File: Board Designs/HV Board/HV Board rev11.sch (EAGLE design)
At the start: 62 parts, among them IC1 OKI-78SR-5, IC2 NE5532SOIC

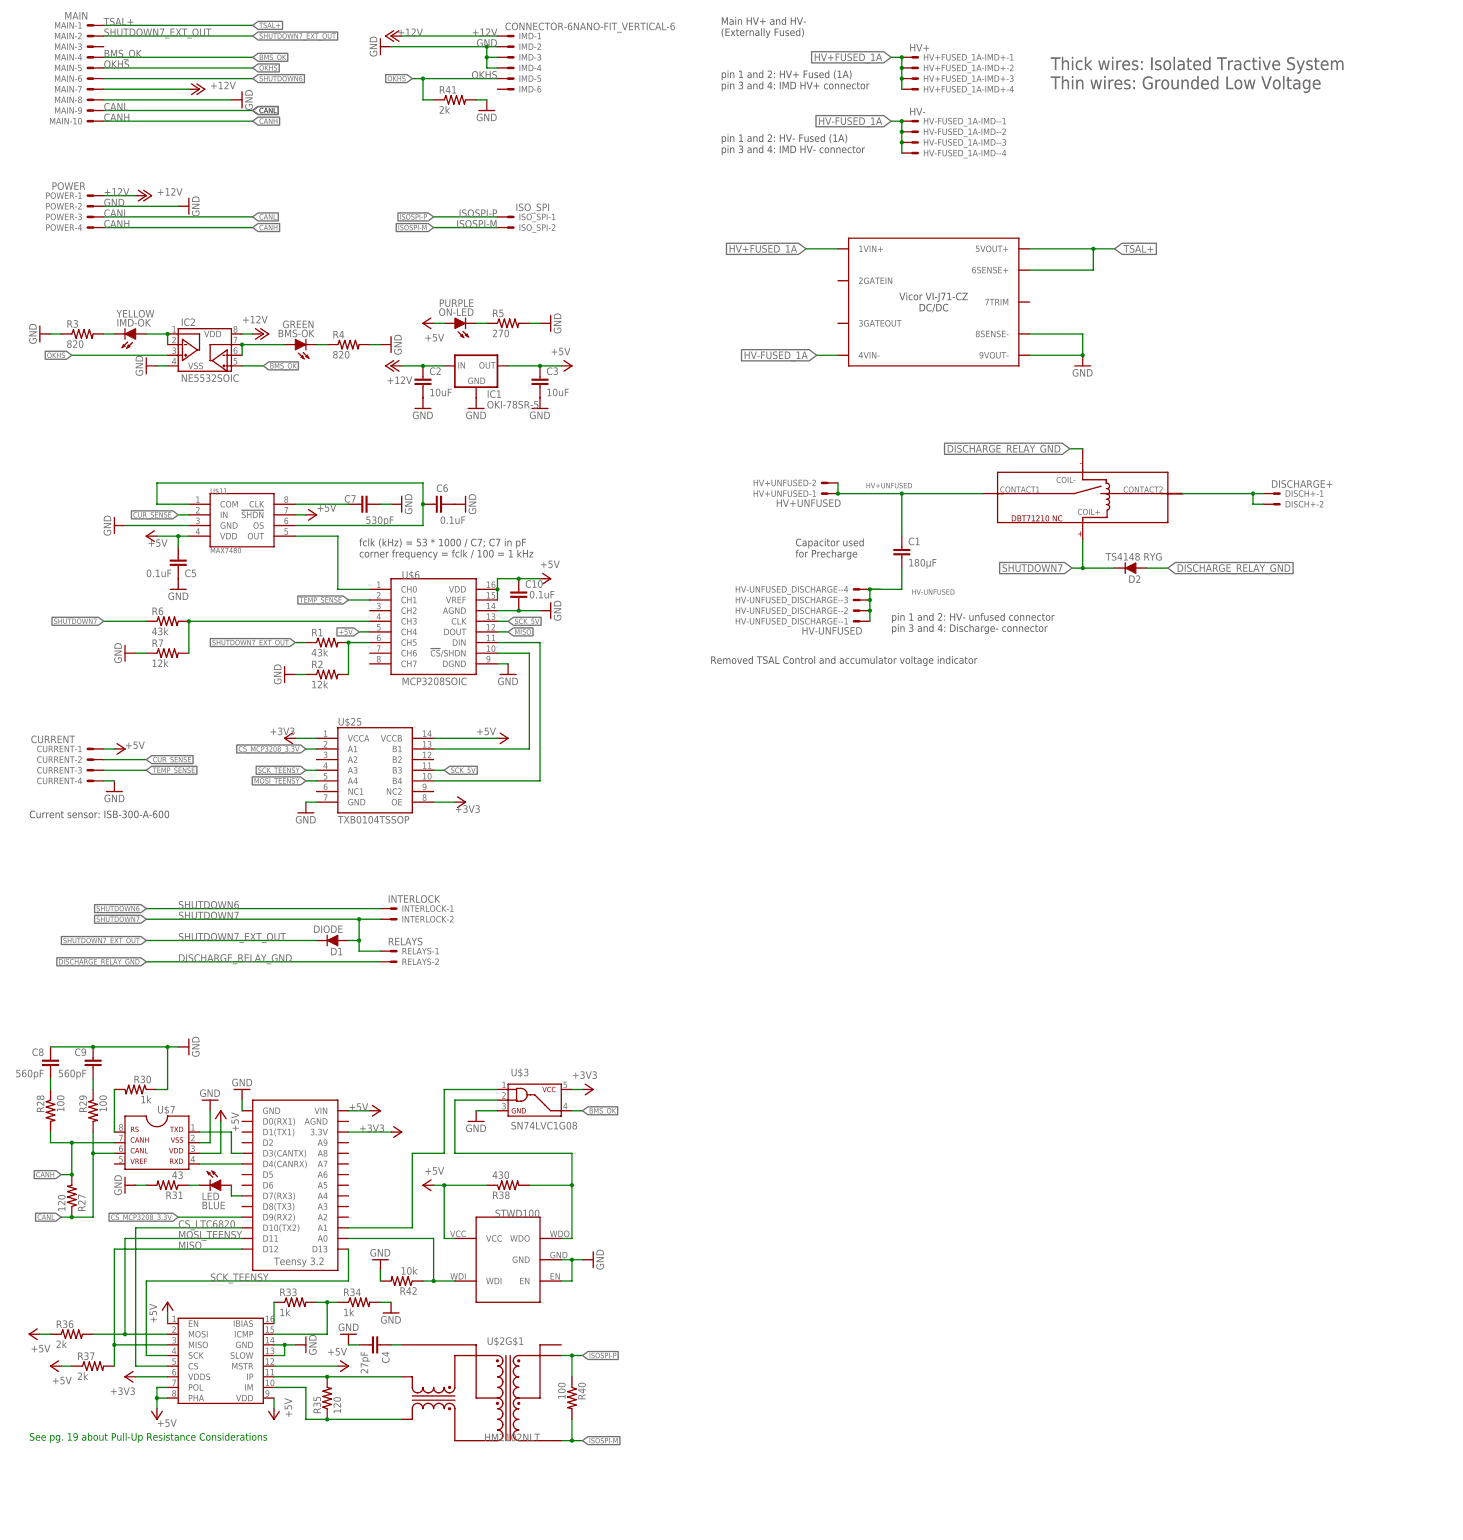
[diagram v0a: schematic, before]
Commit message: HV Board rev11: Update discharge relay holes and pads, change ADC to read shutdown_G, moved silkscreen
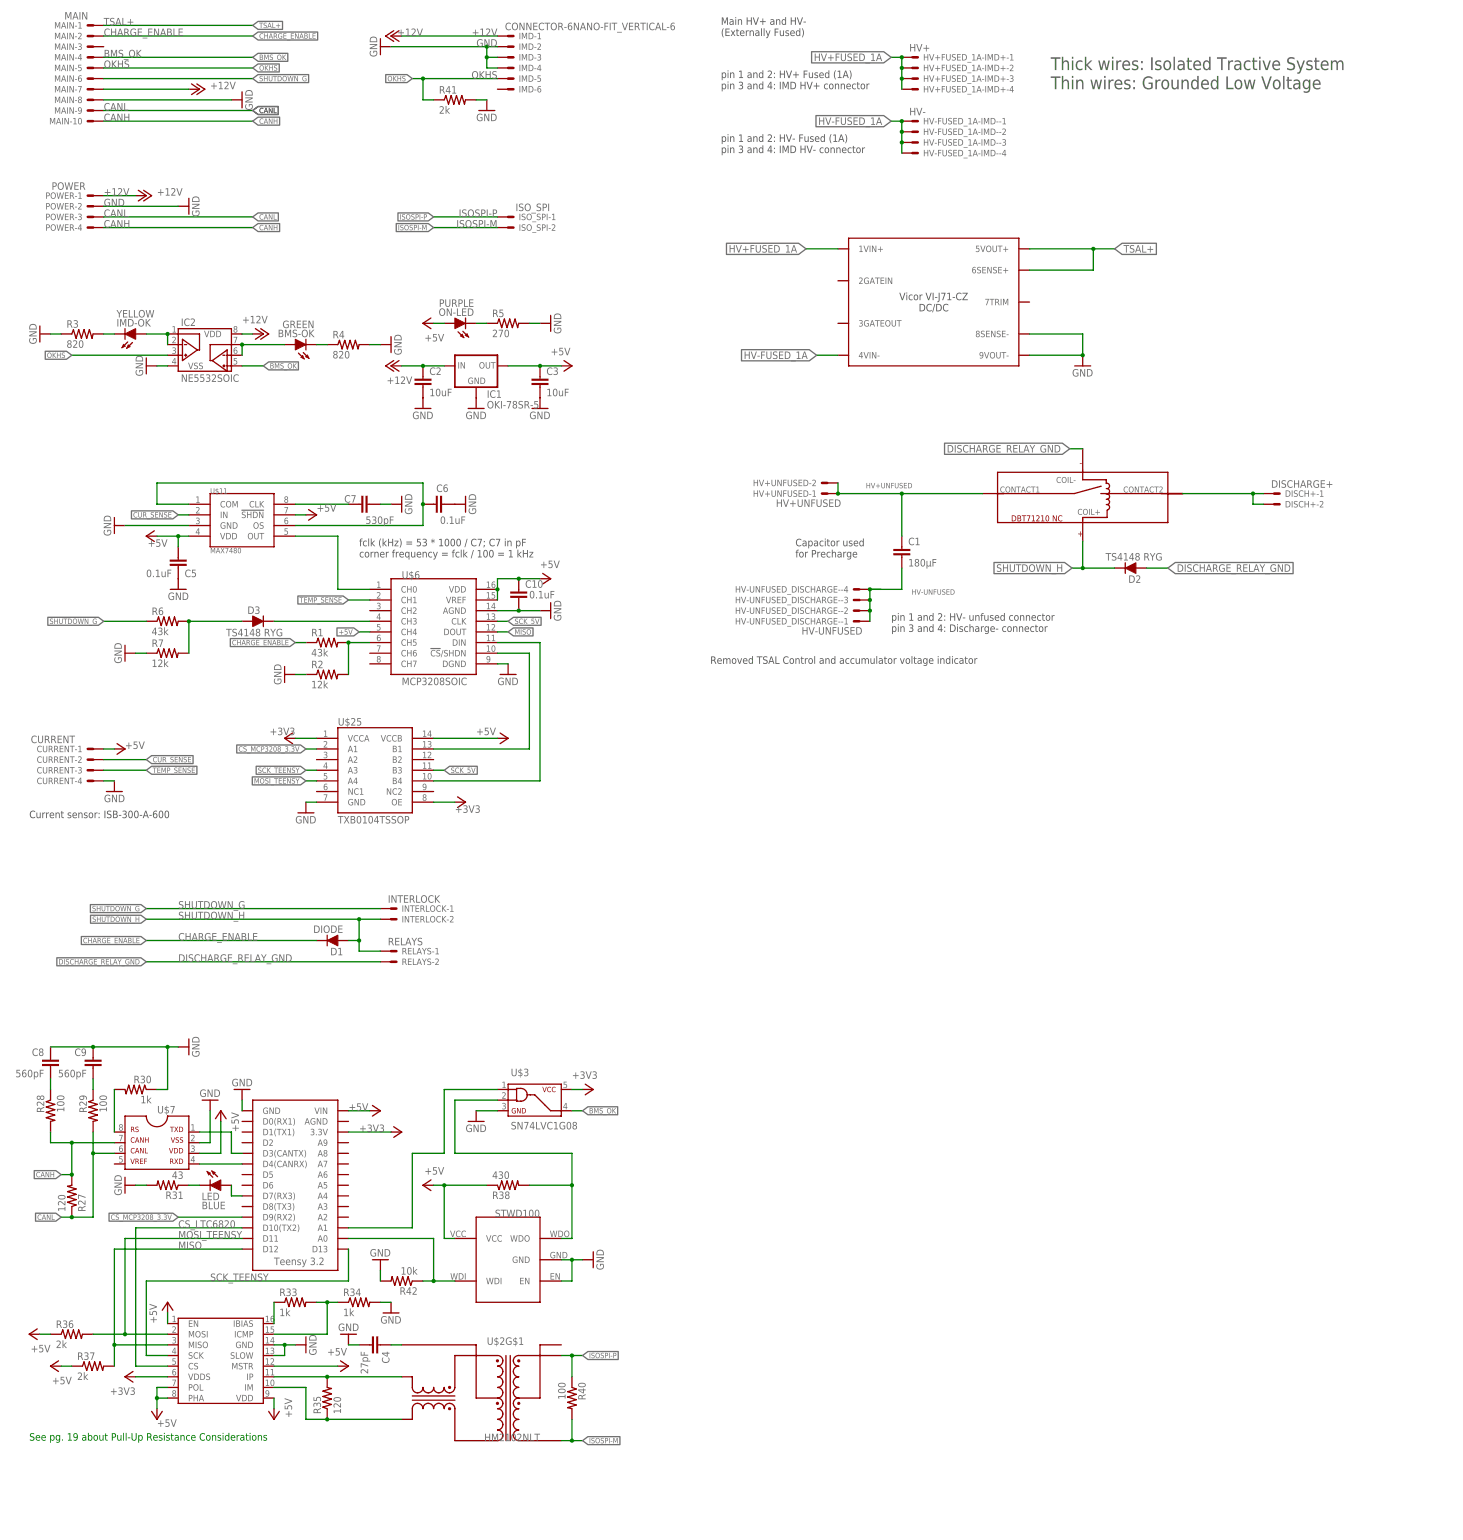
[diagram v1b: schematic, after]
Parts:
- added D3: TS4148 RYG, HyTechDevices:DIODE0805
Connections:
- net SHUTDOWN7_EXT_OUT renamed CHARGE_ENABLE
- removed net SHUTDOWN6: INTERLOCK-1.S, MAIN-6.S
- removed net SHUTDOWN7: D1.A, D2.C, INTERLOCK-2.S, R6.1, RELAYS-1.S, U$4.COIL+
- new net N$10: D3.C, U$6.CH3
- new net SHUTDOWN_G: INTERLOCK-1.S, MAIN-6.S, R6.1
- new net SHUTDOWN_H: D1.A, D2.C, INTERLOCK-2.S, RELAYS-1.S, U$4.COIL+
- net N$9: now also D3.A; no longer U$6.CH3
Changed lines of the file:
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@@
 <part name="GND20" library="supply1" deviceset="GND" device=""/>
 <part name="D2" library="HyTechDevices" deviceset="DIODE" device="0805" value="TS4148 RYG"/>
+<part name="D3" library="HyTechDevices" deviceset="DIODE" device="0805" value="TS4148 RYG"/>
 </parts>
 <sheets>
@@
 <attribute name="VALUE" x="285.75" y="-75.1586" size="1.778" layer="96" rot="R180"/>
 </instance>
+<instance part="D3" gate="1" x="71.12" y="-91.44" smashed="yes">
+<attribute name="NAME" x="67.31" y="-89.6874" size="1.778" layer="95"/>
+<attribute name="VALUE" x="62.23" y="-95.0214" size="1.778" layer="96"/>
+</instance>
 </instances>
 <busses>
@@
 </segment>
 </net>
-<net name="SHUTDOWN7" class="0">
+<net name="SHUTDOWN_H" class="0">
 <segment>
 <wire x1="266.7" y1="-78.74" x2="266.7" y2="-72.26" width="0.1524" layer="91"/>
@@
 <junction x="93.98" y="-167.64"/>
 </segment>
-<segment>
-<pinref part="R6" gate="G$1" pin="1"/>
-<wire x1="43.18" y1="-91.44" x2="33.02" y2="-91.44" width="0.1524" layer="91"/>
-<label x="33.02" y="-91.44" size="1.27" layer="95" rot="R180" xref="yes"/>
-</segment>
-</net>
-<net name="SHUTDOWN6" class="0">
+</net>
+<net name="SHUTDOWN_G" class="0">
 <segment>
 <pinref part="INTERLOCK" gate="-1" pin="S"/>
@@
 <label x="68.58" y="38.1" size="1.27" layer="95" xref="yes"/>
 </segment>
-</net>
-<net name="SHUTDOWN7_EXT_OUT" class="0">
+<segment>
+<pinref part="R6" gate="G$1" pin="1"/>
+<wire x1="43.18" y1="-91.44" x2="33.02" y2="-91.44" width="0.1524" layer="91"/>
+<label x="33.02" y="-91.44" size="1.27" layer="95" rot="R180" xref="yes"/>
+</segment>
+</net>
+<net name="CHARGE_ENABLE" class="0">
 <segment>
 <label x="33.02" y="48.26" size="1.778" layer="95"/>
@@
 <pinref part="R7" gate="G$1" pin="2"/>
 <wire x1="53.34" y1="-99.06" x2="53.34" y2="-91.44" width="0.1524" layer="91"/>
+<pinref part="D3" gate="1" pin="A"/>
+<wire x1="53.34" y1="-91.44" x2="66.04" y2="-91.44" width="0.1524" layer="91"/>
 <junction x="53.34" y="-91.44"/>
+</segment>
+</net>
+<net name="N$10" class="0">
+<segment>
+<pinref part="D3" gate="1" pin="C"/>
 <pinref part="U$6" gate="G$1" pin="CH3"/>
-<wire x1="53.34" y1="-91.44" x2="96.52" y2="-91.44" width="0.1524" layer="91"/>
-</segment>
-</net>
+<wire x1="73.66" y1="-91.44" x2="96.52" y2="-91.44" width="0.1524" layer="91"/>
+</segment>
+</net>

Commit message: HV Board rev11: Amplified BMS_OK signal, added split CAN termination and TVS diode
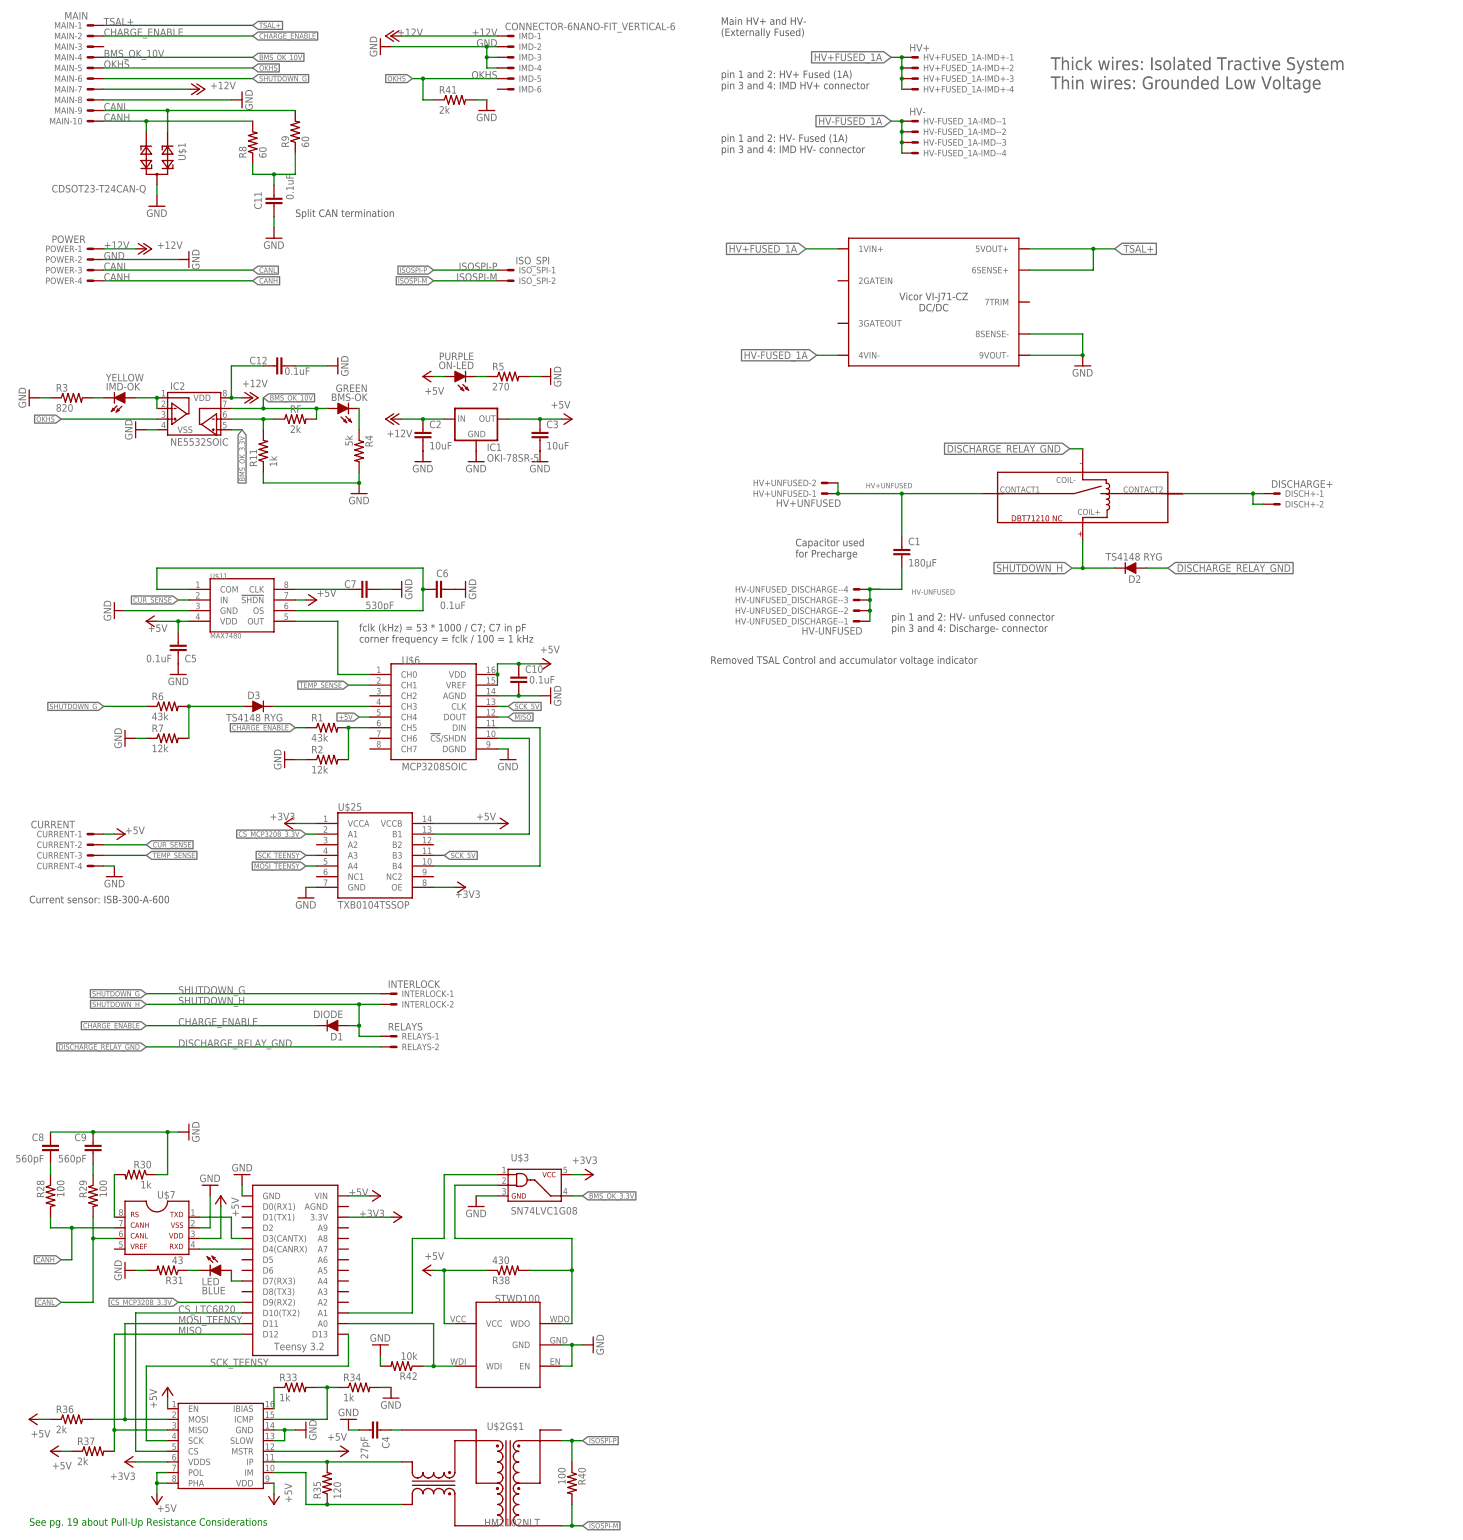
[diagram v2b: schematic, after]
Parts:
- removed R27: 120, HyTechDevices:RESISTOR0805-RES
- added C11, C12: 0.1uF, HyTechDevices:CAP0805
- added R11: 1k, HyTechDevices:RESISTOR0805-RES
- added R8, R9: 60, HyTechDevices:RESISTOR0805-RES
- added RF: 2k, HyTechDevices:RESISTOR0805-RES
- added U$1: CDSOT23-T24CAN-Q, HyTechDevices:CDSOT23-T24CAN-Q
- R4: value 820 -> 5k
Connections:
- removed net BMS_OK: IC2.VINB+, MAIN-4.S, U$3.4
- removed net N$43: BMS-OK.A, IC2.VINB-, IC2.VOUTB
- new net BMS_OK_10V: BMS-OK.A, IC2.VOUTB, MAIN-4.S, RF.2
- new net BMS_OK_3.3V: IC2.VINB+, U$3.4
- new net N$11: C11.2, R8.1, R9.1
- new net N$12: IC2.VINB-, R11.2, RF.1
- net +12V: now also C12.1
- net CANH: now also R8.2, U$1.2; no longer R27.2
- net CANL: now also R9.2, U$1.1; no longer R27.1
- net GND: now also C11.1, C12.2, R11.1, U$1.3
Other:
- note added: "Split CAN termination"
- moved on the sheet: BMS-OK, C10, C2, C3, C4, C5, C6, C7, C8, C9, CURRENT-1, CURRENT-2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
